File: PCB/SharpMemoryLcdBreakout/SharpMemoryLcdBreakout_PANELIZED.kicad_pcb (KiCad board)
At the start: 2 copper layers, 29.9 x 42 mm, 49 parts, among them J1 Pin Header, J2 EMD, J5 FH12-10S-0.5SH

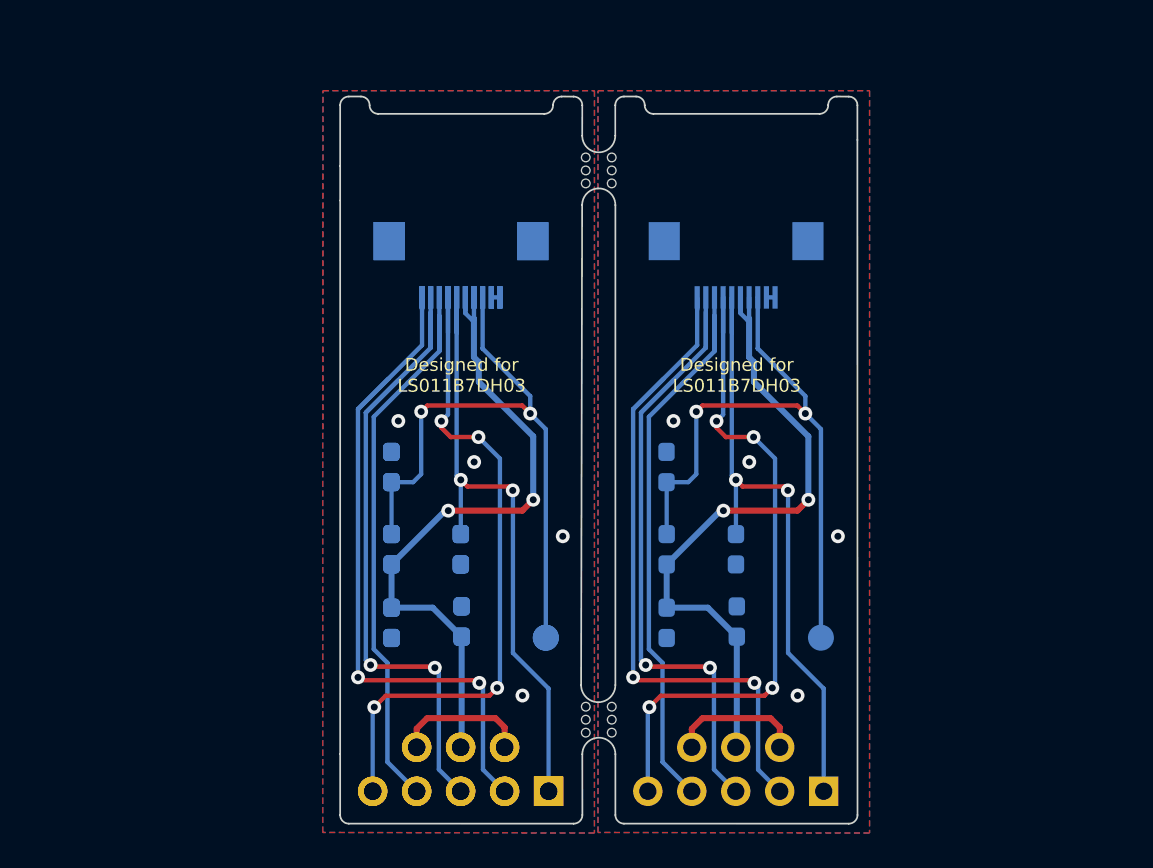
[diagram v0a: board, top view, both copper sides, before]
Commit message: increased part size (0805) and improved silk screen and added ferrite beads
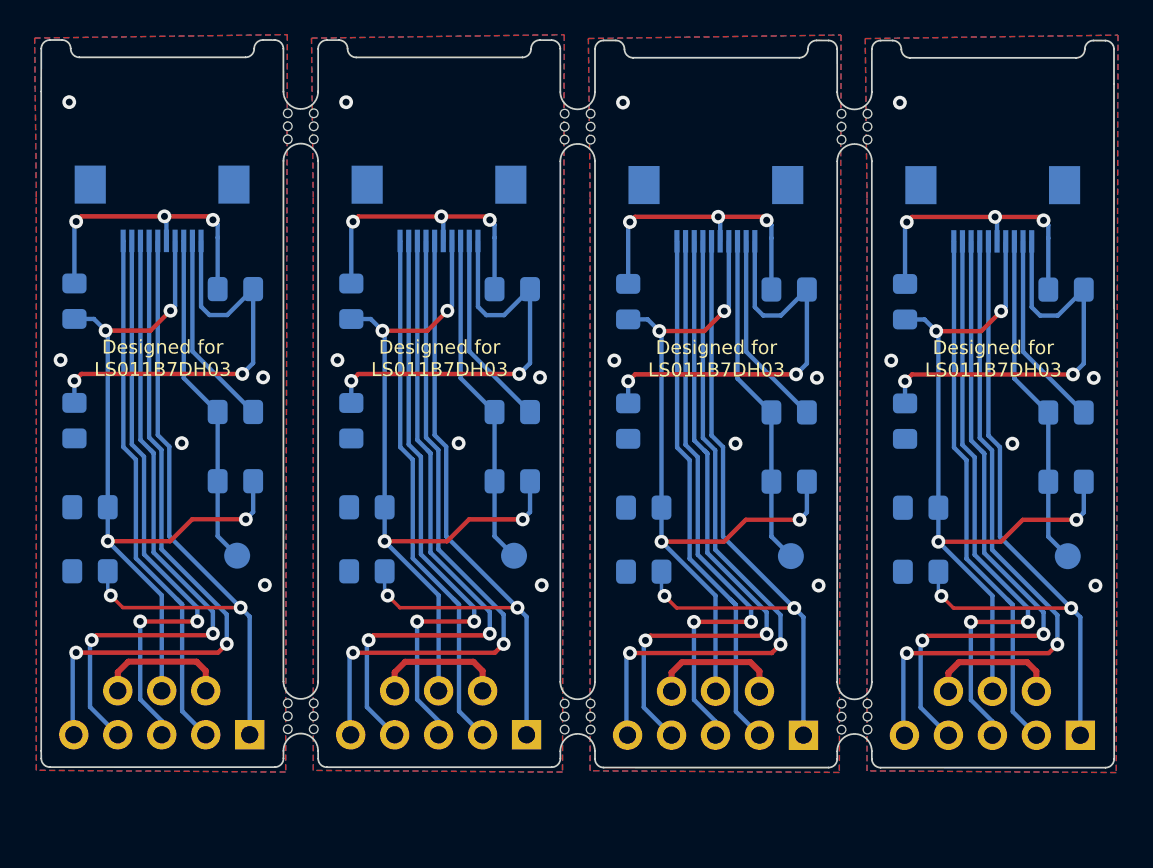
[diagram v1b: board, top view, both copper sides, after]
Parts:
- removed ? (x31): , 
- removed the C1 at (93.7, 62.8)
- removed the C2 at (93.7, 66.9)
- removed the C3 at (89.7, 67.0)
- removed the J1 at (98.7, 76.7)
- removed the J2 at (98.6, 67.9)
- removed the J5 at (93.7, 46.4)
- removed the R1 at (89.7, 58.0)
- removed the R2 at (89.7, 62.8)
- removed the mouse-bite-2mm-slot at (101.6, 40.9)
- removed the mouse-bite-2mm-slot at (101.6, 72.6)
- added C1: 0.1uF, Capacitor_SMD:C_0805_2012Metric_Pad1.15x1.40mm_HandSolder, B.Cu at (88.2, 64.0)
- added C1: 0.1uF, Capacitor_SMD:C_0805_2012Metric_Pad1.15x1.40mm_HandSolder, B.Cu at (72.2, 64.0)
- added C1: 0.1uF, Capacitor_SMD:C_0805_2012Metric_Pad1.15x1.40mm_HandSolder, B.Cu at (104.2, 64.1)
- added C2: 1uF, Capacitor_SMD:C_0805_2012Metric_Pad1.15x1.40mm_HandSolder, B.Cu at (96.6, 47.7)
- added C2: 1uF, Capacitor_SMD:C_0805_2012Metric_Pad1.15x1.40mm_HandSolder, B.Cu at (80.6, 47.7)
- added C2: 1uF, Capacitor_SMD:C_0805_2012Metric_Pad1.15x1.40mm_HandSolder, B.Cu at (112.6, 47.8)
- added C3: 1uF, Capacitor_SMD:C_0805_2012Metric_Pad1.15x1.40mm_HandSolder, B.Cu at (104.2, 60.4)
- added C3: 1uF, Capacitor_SMD:C_0805_2012Metric_Pad1.15x1.40mm_HandSolder, B.Cu at (72.2, 60.3)
- added C3: 1uF, Capacitor_SMD:C_0805_2012Metric_Pad1.15x1.40mm_HandSolder, B.Cu at (88.2, 60.3)
- added FB1: Ferrite_Bead, Resistor_SMD:R_0805_2012Metric_Pad1.15x1.40mm_HandSolder, B.Cu at (103.3, 48.5)
- added FB1: Ferrite_Bead, Resistor_SMD:R_0805_2012Metric_Pad1.15x1.40mm_HandSolder, B.Cu at (87.3, 48.4)
- added FB1: Ferrite_Bead, Resistor_SMD:R_0805_2012Metric_Pad1.15x1.40mm_HandSolder, B.Cu at (71.3, 48.4)
- added FB1: Ferrite_Bead, Resistor_SMD:R_0805_2012Metric_Pad1.15x1.40mm_HandSolder, B.Cu at (119.3, 48.5)
- added FB2: Ferrite_Bead, Resistor_SMD:R_0805_2012Metric_Pad1.15x1.40mm_HandSolder, B.Cu at (103.3, 55.4)
- added FB2: Ferrite_Bead, Resistor_SMD:R_0805_2012Metric_Pad1.15x1.40mm_HandSolder, B.Cu at (71.3, 55.3)
- added FB2: Ferrite_Bead, Resistor_SMD:R_0805_2012Metric_Pad1.15x1.40mm_HandSolder, B.Cu at (87.3, 55.3)
- added FB2: Ferrite_Bead, Resistor_SMD:R_0805_2012Metric_Pad1.15x1.40mm_HandSolder, B.Cu at (119.3, 55.4)
- added J1: Pin Header, SharpMemoryLcdBreakout:PinSocket_2Row_5+3_P2.54mm_Vertical, F.Cu at (81.5, 73.5)
- added J1: Pin Header, SharpMemoryLcdBreakout:PinSocket_2Row_5+3_P2.54mm_Vertical, F.Cu at (97.5, 73.5)
- added J1: Pin Header, SharpMemoryLcdBreakout:PinSocket_2Row_5+3_P2.54mm_Vertical, F.Cu at (113.5, 73.5)
- added J2: EMD, TestPoint:TestPoint_Pad_D1.5mm, B.Cu at (80.7, 63.1)
- added J2: EMD, TestPoint:TestPoint_Pad_D1.5mm, B.Cu at (96.7, 63.1)
- added J2: EMD, TestPoint:TestPoint_Pad_D1.5mm, B.Cu at (112.7, 63.2)
- added J5: FH12-10S-0.5SH, Connector_FFC-FPC:Hirose_FH12-10S-0.5SH_1x10-1MP_P0.50mm_Horizontal, B.Cu at (108.4, 43.1)
- added J5: FH12-10S-0.5SH, Connector_FFC-FPC:Hirose_FH12-10S-0.5SH_1x10-1MP_P0.50mm_Horizontal, B.Cu at (92.4, 43.1)
- added J5: FH12-10S-0.5SH, Connector_FFC-FPC:Hirose_FH12-10S-0.5SH_1x10-1MP_P0.50mm_Horizontal, B.Cu at (76.4, 43.1)
- added R1: 10kΩ, Resistor_SMD:R_0805_2012Metric_Pad1.15x1.40mm_HandSolder, B.Cu at (96.6, 54.8)
- added R1: 10kΩ, Resistor_SMD:R_0805_2012Metric_Pad1.15x1.40mm_HandSolder, B.Cu at (112.6, 54.9)
- added R1: 10kΩ, Resistor_SMD:R_0805_2012Metric_Pad1.15x1.40mm_HandSolder, B.Cu at (80.6, 54.8)
- added R2: 10kΩ, Resistor_SMD:R_0805_2012Metric_Pad1.15x1.40mm_HandSolder, B.Cu at (112.6, 58.9)
- added R2: 10kΩ, Resistor_SMD:R_0805_2012Metric_Pad1.15x1.40mm_HandSolder, B.Cu at (80.6, 58.8)
- added R2: 10kΩ, Resistor_SMD:R_0805_2012Metric_Pad1.15x1.40mm_HandSolder, B.Cu at (96.6, 58.8)
- added mouse-bite-2mm-slot: VAL**, SharpMemoryLcdBreakout:mouse-bite-2mm-slot, F.Cu at (84.4, 72.4)
- added mouse-bite-2mm-slot: VAL**, SharpMemoryLcdBreakout:mouse-bite-2mm-slot, F.Cu at (84.4, 38.3)
- added mouse-bite-2mm-slot: VAL**, SharpMemoryLcdBreakout:mouse-bite-2mm-slot, F.Cu at (100.4, 72.4)
- added mouse-bite-2mm-slot: VAL**, SharpMemoryLcdBreakout:mouse-bite-2mm-slot, F.Cu at (100.4, 38.4)
- added mouse-bite-2mm-slot: VAL**, SharpMemoryLcdBreakout:mouse-bite-2mm-slot, F.Cu at (116.4, 72.4)
- added mouse-bite-2mm-slot: VAL**, SharpMemoryLcdBreakout:mouse-bite-2mm-slot, F.Cu at (116.4, 38.4)
- C1: footprint Capacitor_SMD:C_0603_1608Metric_Pad1.05x0.95mm_HandSolder -> Capacitor_SMD:C_0805_2012Metric_Pad1.15x1.40mm_HandSolder
- C2, C3: value 0.1uF -> 1uF; footprint Capacitor_SMD:C_0603_1608Metric_Pad1.05x0.95mm_HandSolder -> Capacitor_SMD:C_0805_2012Metric_Pad1.15x1.40mm_HandSolder
- R1, R2: footprint Resistor_SMD:R_0603_1608Metric_Pad1.05x0.95mm_HandSolder -> Resistor_SMD:R_0805_2012Metric_Pad1.15x1.40mm_HandSolder
- moved C2 27.0 mm to (128.6, 47.8), turned to 0 degrees
- moved R2 23.4 mm to (128.6, 58.9), turned to 180 degrees
- moved R1 23.3 mm to (128.6, 54.9), turned to 0 degrees
- moved C3 16.1 mm to (120.2, 60.4), turned to 180 degrees
- moved J5 15.2 mm to (124.4, 43.1)
- moved J1 15.2 mm to (129.4, 73.5)
- moved J2 15.0 mm to (128.7, 63.2)
- moved C1 10.7 mm to (120.2, 64.1), turned to 180 degrees
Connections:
- net Net-(C1-Pad1) renamed /DISP
- net Net-(J1-Pad2) renamed /SCLK
- net Net-(J1-Pad3) renamed /SI
- net Net-(J1-Pad4) renamed /SCS
- net Net-(J1-Pad5) renamed /EXTCOMIN
- net Net-(J2-Pad1) renamed /EXTMODE
- C2 pad 1: +3V3 -> VDDA
- C2 pad 2: GND -> GNDA
- J5 pad 10: GND -> GNDA
- J5 pad 6: +3V3 -> VDDA
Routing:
- net GNDA: track 0.00 -> 96.6 mm, vias 0 -> 8
- net +3V3: track 77.6 -> 174.2 mm, vias 4 -> 16
- net /SCS: track 66.6 -> 152.0 mm, vias 0 -> 8
- net /DISP: track 74.6 -> 160.0 mm, vias 4 -> 8
- net /EXTCOMIN: track 79.3 -> 156.0 mm
- net VDDA: track 0.00 -> 69.2 mm, vias 0 -> 12
- net GND: track 16.5 -> 76.4 mm, vias 8 -> 20
- net /SI: track 78.2 -> 135.7 mm, vias 4 -> 8
- net /SCLK: track 81.4 -> 123.8 mm, vias 4 -> 0
- net /EXTMODE: track 72.9 -> 77.9 mm, vias 4 -> 0
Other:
- board size 29.9 x 42 mm -> 62 x 42 mm
- board text added: "Sharp Memory LCD Breakout v0.3"
- board text removed: "Sharp Memory LCD Breakout v0.2"
